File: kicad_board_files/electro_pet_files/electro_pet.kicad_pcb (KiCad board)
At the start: 2 copper layers, 42 x 63.8 mm, 20 parts, among them M3_bolt_nut_custom VAL**, SW1 SWITCH_INV, SW2 SW_PUSH, SW3 SW_PUSH, U1 8X8_LED_MATRIX, U2 LIPO_CHARGER, U3 ELECTRO_HAT, U4 3.3_V_REG, U5 MPU-6050, U6 DC_DC_BOOST, U7 ARDUINO_PRO_MICRO, U8 BATTERY_CUSTOM, U9 A3144

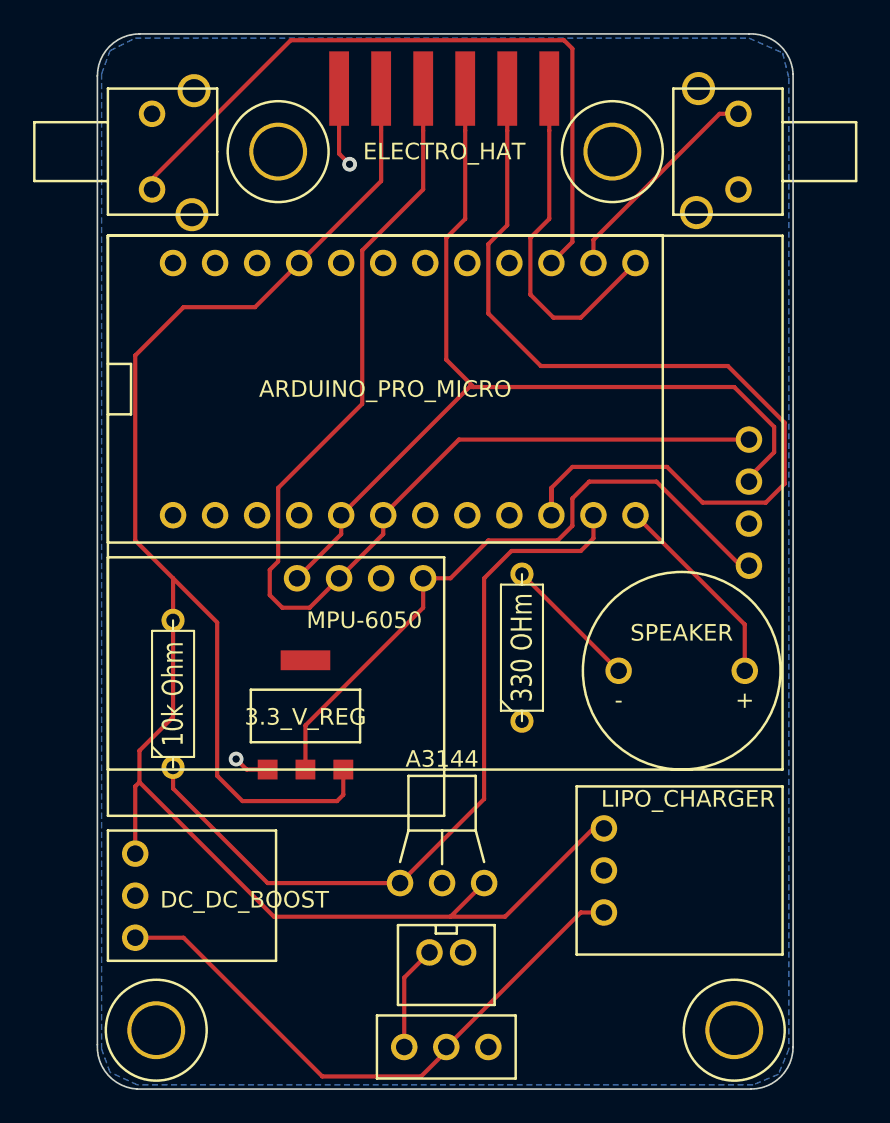
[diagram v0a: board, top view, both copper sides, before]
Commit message: Added the fixes for the battery
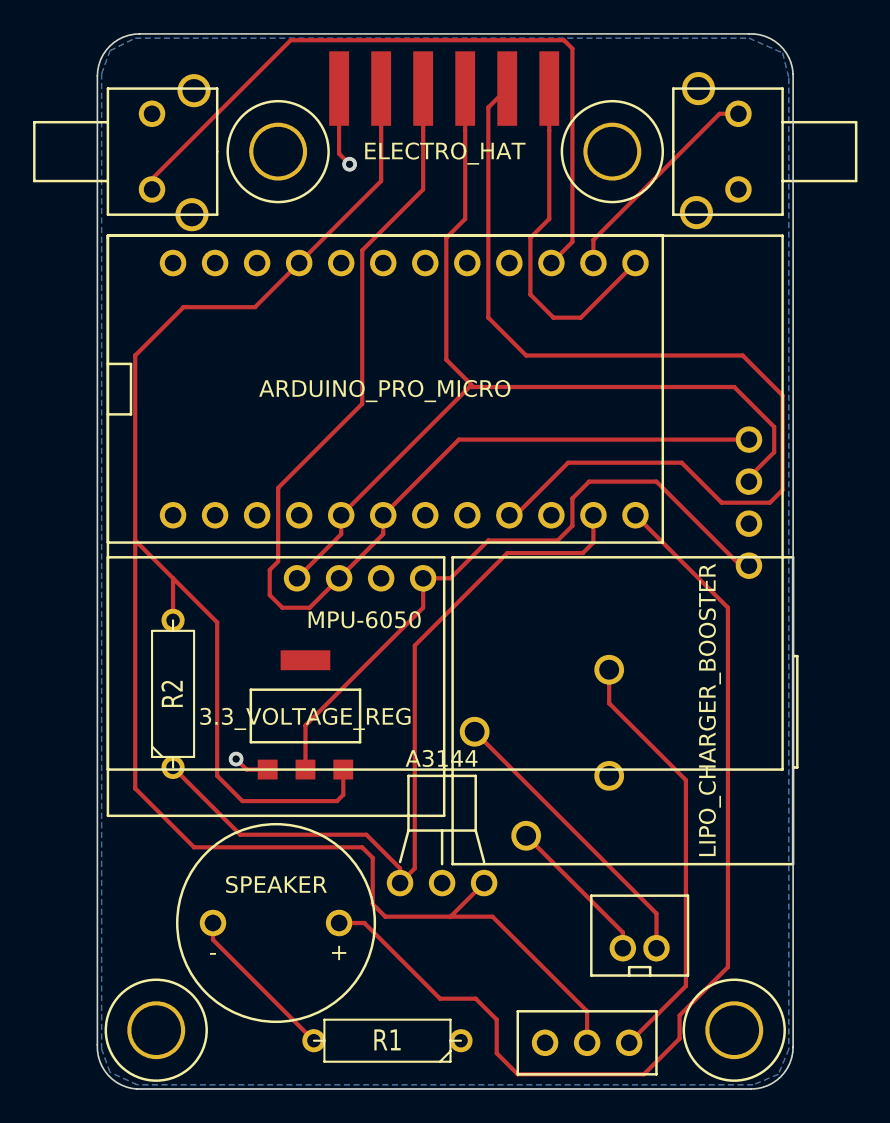
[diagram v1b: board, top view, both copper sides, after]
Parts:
- removed 10k Ohm: R, R3-5
- removed 330 OHm: R, R3-5
- removed U6: DC_DC_BOOST, small_DC_DC_boost
- added R1: R, R3-5, F.Cu at (298.7, 103.1)
- added R2: R, R3-5, F.Cu at (285.8, 82.2)
- U2: value LIPO_CHARGER -> LIPO_CHARGER_BOOSTER; footprint small_lipo_charger -> lipo_charger_booster
- U4: value 3.3_V_REG -> 3.3_VOLTAGE_REG
- moved SP1 28.9 mm to (292.0, 96.0)
- moved U8 11.8 mm to (313.9, 96.8), turned to 0 degrees
- moved U2 10.2 mm to (312.9, 83.2)
- moved SW1 8.51 mm to (310.8, 103.3), turned to 180 degrees
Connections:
- SW1 pad 1: N-0000010 -> N-000009
- SW1 pad 2: N-0000026 -> N-0000022
- SW2 pad 2: N-000008 -> N-0000010
- SW3 pad 2: N-000008 -> N-0000010
- U1 pad 3: N-000008 -> N-0000010
- U2 pad 1: N-0000023 (its old number) -> N-000008
- U2 pad 2: N-000008 -> N-000007
- U2 pad 3: N-0000026 -> N-0000010
- U3 pad 1: N-000008 -> N-0000010
- U3 pad 2: N-0000023 (its old number) -> N-0000022
- U3 pad 5: N-0000017 -> N-000001
- U4 pad 1: N-000008 -> N-0000010
- U4 pad 3: N-0000023 (its old number) -> N-0000022
- U5 pad 2: N-000008 -> N-0000010
- U7 pad 10: N-0000017 -> (no net)
- U7 pad 21: N-0000023 (its old number) -> (no net)
- U7 pad 23: N-000008 -> N-0000010
- U7 pad 9: (no net) -> N-000001
- U8 pad 2: N-0000010 -> N-000007
- U9 pad 1: N-0000023 (its old number) -> N-0000022
- U9 pad 2: N-000008 -> N-0000010
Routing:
- net N-0000022: track 0.00 -> 119.0 mm
- net N-0000023 (its old number): track 116.3 -> 0.00 mm
- net N-000001: track 0.00 -> 58.9 mm
- net N-0000017: track 57.7 -> 0.00 mm
- net N-000003: track 12.1 -> 61.6 mm
- net N-0000026: track 36.0 -> 0.00 mm
- net N-000009: track 0.00 -> 25.9 mm
- net N-000007: track 0.00 -> 17.6 mm
- net N-000008: track 7.00 -> 9.21 mm, vias 2 -> 0
- net N-000004: track 8.26 -> 9.64 mm
- net N-0000010: track 6.35 -> 7.00 mm, vias 0 -> 2
- added copper zone on B.Cu, net N-0000010
- removed copper zone on B.Cu, net N-000008
